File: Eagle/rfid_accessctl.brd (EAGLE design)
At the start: 50 x 40 mm, 21 parts

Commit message: Start v1.2 board version
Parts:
- removed U$1: V_REG_LD1117VXX, SparkFun-PowerIC:78XXL
- added D1, D2: (no value), SparkFun-DiscreteSemi:SMA-DIODE
- added JMP1: 0R-JUMPB, jump-0r-smd:B0R-JMP
- added Q1: IRLL014, Misc_Transistors:SOT-223
- added R6: (no value), SparkFun-Resistors:0805
- added VR1: UA78M33CDCY, TI-UA78M33CDCY:SOT230P700X180-4N
- C1: value (none) -> 0.33uF; device SparkFun-Capacitors:CPOL-RADIAL-10UF-25V-KIT -> SparkFun-Capacitors:0805
- C2: value (none) -> 0.1uF; device SparkFun-Capacitors:CAP-PTH-SMALL-KIT -> SparkFun-Capacitors:0805
- R5: value 470 -> 4.7k
- moved RELAY_HEADER 30.2 mm to (9.53, 10.2)
- moved C1 15.9 mm to (3.81, 16.5)
- moved C2 13.1 mm to (8.89, 16.5), turned to 180 degrees
- moved I2C_CONN 2.54 mm to (15.2, 30.5)
- moved R2 1.27 mm to (41.9, 20.3)
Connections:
- new net RELAY_OP: D2.A, Q1.2, RELAY_HEADER.1
- new net RELAY_PWR: D2.C, JMP1.2, RELAY_HEADER.3
- net GND: now also D1.A, LED_HEADER.3, Q1.3, R6.1, VR1.2, VR1.4; no longer LED_HEADER.2, U$1.IN
- net PWR_IN: now also C1.1, D1.C, JMP1.3, VR1.1; no longer C2.1, RELAY_HEADER.3, U$1.OUT
- net RELAY_CTL: now also Q1.1, R6.2; no longer RELAY_HEADER.1
- net VCC: now also C2.1, JMP1.1, LED_HEADER.2, VR1.3; no longer C1.1, LED_HEADER.3, U$1.GND
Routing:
- net GND: track 6.34 -> 26.2 mm, vias 1 -> 4
- net RELAY_OP: track 0.00 -> 17.3 mm, vias 0 -> 1
- net RELAY_PWR: track 0.00 -> 11.3 mm
- net PWR_IN: track 32.5 -> 21.7 mm, vias 1 -> 0
- net RELAY_CTL: track 22.9 -> 29.1 mm, vias 0 -> 2
- net SCL: track 34.7 -> 40.1 mm, vias 0 -> 2
- net VCC: track 109.0 -> 112.2 mm
- net SDA: track 31.1 -> 28.5 mm
- net PGM_CTL: track 4.76 -> 5.80 mm
- net RFID_SCK: track 18.9 -> 18.4 mm
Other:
- board text added: "3v3"
- board text added: "Access Controller V1.2"
- board text added: "Di"
- board text added: "JP1"
- board text added: "PWR_IN"
- board text added: "S'NOID/RLY"
- board text removed: "3v"
- board text removed: "Access Controller V1.1"
- board text removed: "DATA"
- board text removed: "PWR"
- board text removed: "RELAY"

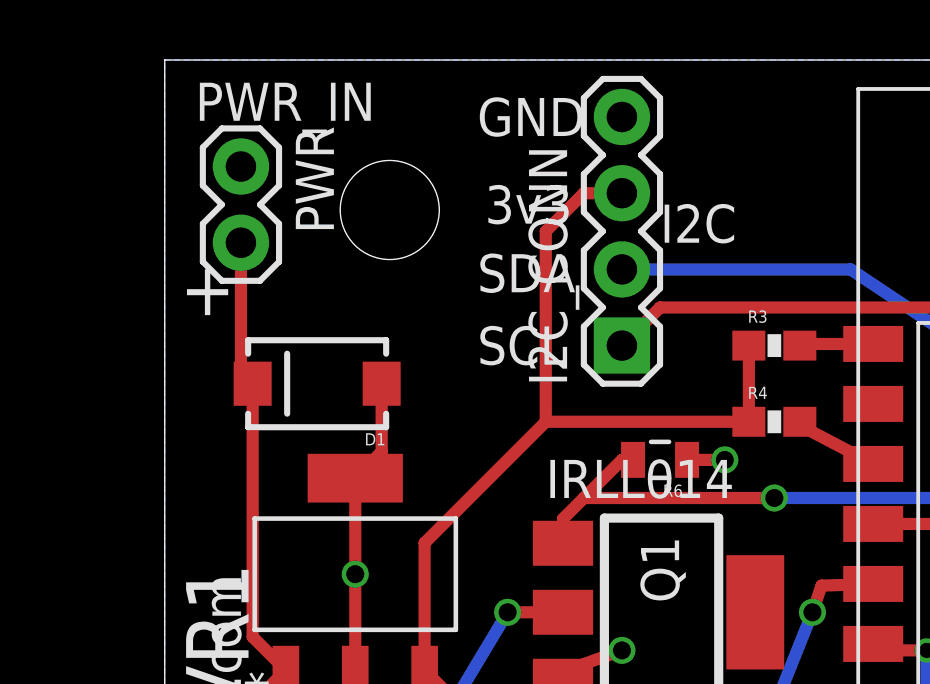
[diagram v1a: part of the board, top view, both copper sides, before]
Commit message: Updates for 0603
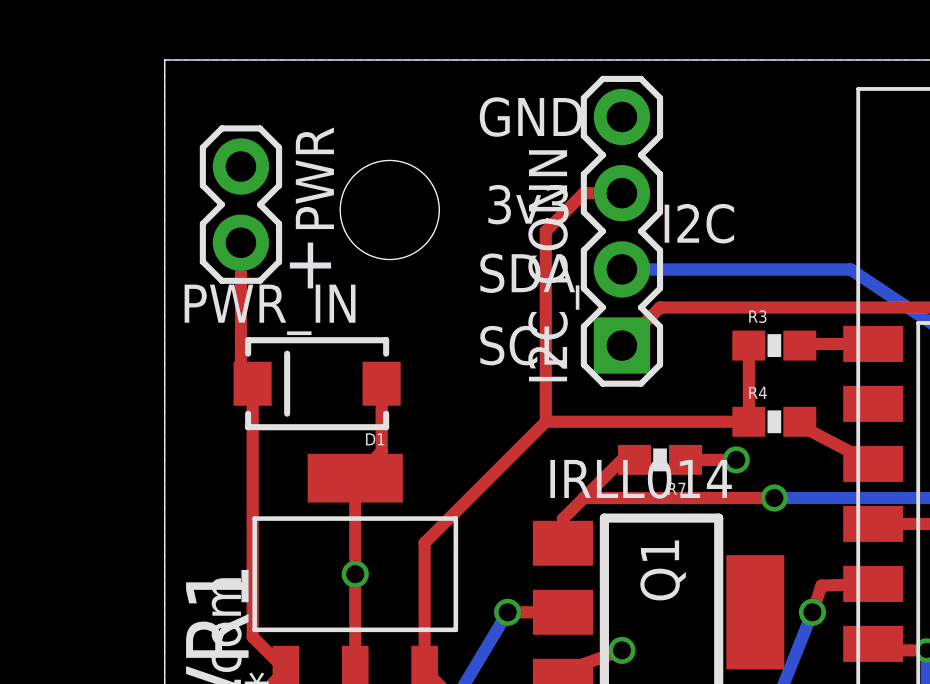
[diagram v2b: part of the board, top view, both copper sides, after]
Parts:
- removed R6: (no value), SparkFun-Resistors:0805
- added R7: (no value), SparkFun-Passives:0603-RES
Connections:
- net GND: now also R7.1; no longer R6.1
- net RELAY_CTL: now also R7.2; no longer R6.2
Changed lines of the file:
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@@
 <text x="32.385" y="9.271" size="1.27" layer="21" font="vector" ratio="15" rot="R90">RST</text>
 <text x="27.178" y="9.271" size="1.27" layer="21" font="vector" ratio="15" rot="R90">IRQ</text>
-<text x="1.016" y="37.973" size="1.27" layer="21" font="vector" ratio="15">PWR_IN</text>
-<text x="0.508" y="31.496" size="1.778" layer="21" font="vector" ratio="15">+</text>
+<text x="0.508" y="31.242" size="1.27" layer="21" font="vector" ratio="15">PWR_IN</text>
+<text x="3.937" y="32.385" size="1.778" layer="21" font="vector" ratio="15">+</text>
 <text x="3.048" y="7.239" size="1.27" layer="21" font="vector" ratio="15">S'NOID/RLY</text>
 <text x="16.51" y="33.909" size="1.27" layer="21" font="vector" ratio="15">I2C</text>
@@
 <element name="D1" library="SparkFun-DiscreteSemi" package="SMA-DIODE" value="" x="5.08" y="29.21" rot="R180"/>
 <element name="D2" library="SparkFun-DiscreteSemi" package="SMA-DIODE" value="" x="12.7" y="11.43" rot="R90"/>
-<element name="R6" library="SparkFun-Resistors" package="0805" value="" x="16.51" y="26.67" rot="R180"/>
+<element name="R7" library="SparkFun-Passives" package="0603-RES" value="" x="16.51" y="26.67" rot="R180"/>
 </elements>
 <signals>
@@
 <wire x1="6.35" y1="22.86" x2="6.35" y2="26.0604" width="0.4064" layer="1"/>
 <contactref element="RELAY_HEADER" pad="2"/>
-<contactref element="R6" pad="1"/>
-<via x="18.669" y="26.67" extent="1-16" drill="0.6"/>
-<wire x1="17.41" y1="26.67" x2="18.669" y2="26.67" width="0.4064" layer="1"/>
 <contactref element="LED_HEADER" pad="3"/>
+<contactref element="R7" pad="1"/>
+<via x="19.05" y="26.67" extent="1-16" drill="0.6"/>
+<wire x1="17.36" y1="26.67" x2="19.05" y2="26.67" width="0.4064" layer="1"/>
 </signal>
 <signal name="PWR_IN">
@@
 <wire x1="13.97" y1="25.4" x2="13.275" y2="24.705" width="0.4064" layer="1"/>
 <wire x1="13.275" y1="24.705" x2="13.275" y2="23.89" width="0.4064" layer="1"/>
-<contactref element="R6" pad="2"/>
-<wire x1="15.61" y1="26.67" x2="15.24" y2="26.67" width="0.4064" layer="1"/>
+<contactref element="R7" pad="2"/>
+<wire x1="15.66" y1="26.67" x2="15.24" y2="26.67" width="0.4064" layer="1"/>
 <wire x1="15.24" y1="26.67" x2="13.97" y2="25.4" width="0.4064" layer="1"/>
 </signal>

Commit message: Add DIP switches on serial lines (optional)
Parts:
- added SW1: (no value), SparkFun-Electromechanical:DIPSWITCH-02-50MIL
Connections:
- net GND: now also SW1.3, SW1.4
- net RXD: now also SW1.1
- net TXD: now also SW1.2
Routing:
- net TXD: track 11.8 -> 32.3 mm, vias 0 -> 2
- net RXD: track 11.5 -> 28.9 mm, vias 0 -> 2
- net GND: track 26.6 -> 29.3 mm, vias 4 -> 5
- net VCC: track 112.2 -> 114.0 mm, vias 2 -> 1
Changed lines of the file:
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@@
 <element name="D2" library="SparkFun-DiscreteSemi" package="SMA-DIODE" value="" x="12.7" y="11.43" rot="R90"/>
 <element name="R7" library="SparkFun-Passives" package="0603-RES" value="" x="16.51" y="26.67" rot="R180"/>
+<element name="SW1" library="SparkFun-Electromechanical" package="DIPSWITCH-02-50MIL" value="" x="38.1" y="10.16" rot="R180"/>
 </elements>
 <signals>
@@
 <via x="19.05" y="26.67" extent="1-16" drill="0.6"/>
 <wire x1="17.36" y1="26.67" x2="19.05" y2="26.67" width="0.4064" layer="1"/>
+<contactref element="SW1" pad="4"/>
+<contactref element="SW1" pad="3"/>
+<wire x1="38.735" y1="6.46" x2="38.1" y2="6.46" width="0.4064" layer="1"/>
+<via x="38.1" y="5.08" extent="1-16" drill="0.6"/>
+<wire x1="38.1" y1="6.46" x2="37.465" y2="6.46" width="0.4064" layer="1"/>
+<wire x1="38.1" y1="5.08" x2="38.1" y2="6.46" width="0.4064" layer="1"/>
 </signal>
 <signal name="PWR_IN">
@@
 <contactref element="RFID_CONN" pad="8"/>
 <wire x1="19.47" y1="30.48" x2="19.47" y2="27.94" width="0.4064" layer="1"/>
-<via x="34.29" y="15.24" extent="1-16" drill="0.508"/>
-<wire x1="48.26" y1="30.48" x2="46.99" y2="30.48" width="0.4064" layer="1"/>
-<wire x1="46.99" y1="30.48" x2="44.45" y2="27.94" width="0.4064" layer="1"/>
-<wire x1="44.45" y1="27.94" x2="44.45" y2="24.13" width="0.4064" layer="1"/>
-<via x="44.45" y="24.13" extent="1-16" drill="0.508"/>
-<wire x1="44.45" y1="24.13" x2="44.45" y2="17.78" width="0.4064" layer="16"/>
-<wire x1="44.45" y1="17.78" x2="45.72" y2="16.51" width="0.4064" layer="16"/>
-<wire x1="45.72" y1="16.51" x2="48.26" y2="16.51" width="0.4064" layer="16"/>
 <contactref element="X1" pad="8"/>
 <contactref element="I2C_CONN" pad="3"/>
-<wire x1="34.29" y1="6.35" x2="34.29" y2="15.24" width="0.4064" layer="1"/>
-<wire x1="23.615" y1="16.535" x2="25.375" y2="16.535" width="0.4064" layer="1"/>
-<wire x1="25.375" y1="16.535" x2="29.21" y2="15.24" width="0.4064" layer="1"/>
-<wire x1="29.21" y1="15.24" x2="34.29" y2="15.24" width="0.4064" layer="1"/>
 <contactref element="R5" pad="2"/>
-<wire x1="44.45" y1="17.78" x2="44.45" y2="15.24" width="0.4064" layer="16"/>
-<wire x1="44.45" y1="15.24" x2="41.91" y2="15.24" width="0.4064" layer="16"/>
-<wire x1="41.91" y1="15.24" x2="34.29" y2="15.24" width="0.4064" layer="16"/>
-<wire x1="42.887" y1="24.638" x2="43.942" y2="24.638" width="0.4064" layer="1"/>
-<wire x1="43.942" y1="24.638" x2="44.45" y2="24.13" width="0.4064" layer="1"/>
 <contactref element="VR1" pad="3"/>
 <contactref element="C2" pad="1"/>
@@
 <wire x1="8.6614" y1="23.9014" x2="12.7" y2="27.94" width="0.4064" layer="1"/>
 <contactref element="LED_HEADER" pad="2"/>
-<wire x1="48.26" y1="10.16" x2="45.72" y2="10.16" width="0.4064" layer="16"/>
-<wire x1="45.72" y1="10.16" x2="41.91" y2="13.97" width="0.4064" layer="16"/>
-<wire x1="41.91" y1="13.97" x2="41.91" y2="15.24" width="0.4064" layer="16"/>
+<wire x1="23.615" y1="16.535" x2="30.455" y2="16.535" width="0.4064" layer="1"/>
+<wire x1="30.455" y1="16.535" x2="34.29" y2="12.7" width="0.4064" layer="1"/>
+<wire x1="34.29" y1="12.7" x2="34.29" y2="6.35" width="0.4064" layer="1"/>
+<wire x1="48.26" y1="10.16" x2="38.1" y2="10.16" width="0.4064" layer="1"/>
+<wire x1="38.1" y1="10.16" x2="34.29" y2="6.35" width="0.4064" layer="1"/>
+<wire x1="48.26" y1="10.16" x2="46.99" y2="10.16" width="0.4064" layer="16"/>
+<wire x1="46.99" y1="10.16" x2="45.72" y2="11.43" width="0.4064" layer="16"/>
+<wire x1="45.72" y1="11.43" x2="45.72" y2="15.24" width="0.4064" layer="16"/>
+<wire x1="45.72" y1="15.24" x2="46.99" y2="16.51" width="0.4064" layer="16"/>
+<wire x1="46.99" y1="16.51" x2="48.26" y2="16.51" width="0.4064" layer="16"/>
+<wire x1="48.26" y1="30.48" x2="46.99" y2="30.48" width="0.4064" layer="1"/>
+<wire x1="46.99" y1="30.48" x2="43.18" y2="26.67" width="0.4064" layer="1"/>
+<wire x1="43.18" y1="26.67" x2="43.18" y2="24.931" width="0.4064" layer="1"/>
+<wire x1="43.18" y1="24.931" x2="42.887" y2="24.638" width="0.4064" layer="1"/>
+<wire x1="42.887" y1="24.638" x2="45.212" y2="24.638" width="0.4064" layer="1"/>
+<wire x1="45.212" y1="24.638" x2="45.72" y2="24.13" width="0.4064" layer="1"/>
+<wire x1="45.72" y1="24.13" x2="45.72" y2="20.32" width="0.4064" layer="1"/>
+<via x="45.72" y="20.32" extent="1-16" drill="0.6"/>
+<wire x1="45.72" y1="20.32" x2="45.72" y2="19.05" width="0.4064" layer="16"/>
+<wire x1="45.72" y1="19.05" x2="48.26" y2="16.51" width="0.4064" layer="16"/>
 </signal>
 <signal name="DTR">
@@
 <signal name="RXD">
 <contactref element="FTDI_CONN" pad="TXO"/>
+<wire x1="43.775" y1="28.535" x2="48.26" y2="33.02" width="0.4064" layer="1"/>
+<contactref element="SW1" pad="1"/>
 <contactref element="X1" pad="15"/>
-<wire x1="38.615" y1="28.535" x2="43.775" y2="28.535" width="0.4064" layer="1"/>
-<wire x1="43.775" y1="28.535" x2="48.26" y2="33.02" width="0.4064" layer="1"/>
+<wire x1="43.775" y1="28.535" x2="38.615" y2="28.535" width="0.4064" layer="1"/>
+<wire x1="38.615" y1="28.535" x2="37.425" y2="28.535" width="0.4064" layer="1"/>
+<wire x1="37.425" y1="28.535" x2="36.83" y2="27.94" width="0.4064" layer="1"/>
+<via x="36.83" y="27.94" extent="1-16" drill="0.6"/>
+<wire x1="36.83" y1="27.94" x2="36.83" y2="24.13" width="0.4064" layer="16"/>
+<wire x1="36.83" y1="24.13" x2="38.1" y2="22.86" width="0.4064" layer="16"/>
+<wire x1="38.1" y1="22.86" x2="38.1" y2="16.51" width="0.4064" layer="16"/>
+<wire x1="38.1" y1="16.51" x2="39.37" y2="15.24" width="0.4064" layer="16"/>
+<via x="39.37" y="15.24" extent="1-16" drill="0.6"/>
+<wire x1="39.37" y1="15.24" x2="39.37" y2="14.495" width="0.4064" layer="1"/>
+<wire x1="39.37" y1="14.495" x2="38.735" y2="13.86" width="0.4064" layer="1"/>
 </signal>
 <signal name="TXD">
 <contactref element="FTDI_CONN" pad="RXI"/>
-<contactref element="X1" pad="16"/>
-<wire x1="38.615" y1="30.535" x2="43.125" y2="30.535" width="0.4064" layer="1"/>
 <wire x1="43.125" y1="30.535" x2="43.18" y2="30.48" width="0.4064" layer="1"/>
 <wire x1="43.18" y1="30.48" x2="48.26" y2="35.56" width="0.4064" layer="1"/>
+<contactref element="X1" pad="16"/>
+<contactref element="SW1" pad="2"/>
+<wire x1="43.125" y1="30.535" x2="38.615" y2="30.535" width="0.4064" layer="1"/>
+<wire x1="38.615" y1="30.535" x2="35.615" y2="30.535" width="0.4064" layer="1"/>
+<wire x1="35.615" y1="30.535" x2="35.56" y2="30.48" width="0.4064" layer="1"/>
+<via x="35.56" y="30.48" extent="1-16" drill="0.6"/>
+<wire x1="35.56" y1="30.48" x2="35.56" y2="22.86" width="0.4064" layer="16"/>
+<wire x1="35.56" y1="22.86" x2="36.83" y2="21.59" width="0.4064" layer="16"/>
+<wire x1="36.83" y1="21.59" x2="36.83" y2="15.24" width="0.4064" layer="16"/>
+<via x="36.83" y="15.24" extent="1-16" drill="0.6"/>
+<wire x1="36.83" y1="15.24" x2="36.83" y2="14.495" width="0.4064" layer="1"/>
+<wire x1="36.83" y1="14.495" x2="37.465" y2="13.86" width="0.4064" layer="1"/>
 </signal>
 <signal name="PGM_CTL">
@@
 <contactref element="Q1" pad="1"/>
 <via x="20.32" y="25.4" extent="1-16" drill="0.6"/>
-<wire x1="20.32" y1="25.4" x2="31.75" y2="25.4" width="0.4064" layer="16"/>
-<via x="31.75" y="25.4" extent="1-16" drill="0.6"/>
-<wire x1="31.75" y1="25.4" x2="32.885" y2="26.535" width="0.4064" layer="1"/>
+<wire x1="20.32" y1="25.4" x2="30.48" y2="25.4" width="0.4064" layer="16"/>
+<via x="30.48" y="25.4" extent="1-16" drill="0.6"/>
+<wire x1="30.48" y1="25.4" x2="32.885" y2="26.535" width="0.4064" layer="1"/>
 <wire x1="32.885" y1="26.535" x2="38.615" y2="26.535" width="0.4064" layer="1"/>
 <wire x1="20.32" y1="25.4" x2="13.97" y2="25.4" width="0.4064" layer="1"/>
@@
 <signal name="SDA">
 <contactref element="I2C_CONN" pad="2"/>
-<wire x1="15.24" y1="33.02" x2="22.86" y2="33.02" width="0.4064" layer="16"/>
-<wire x1="22.86" y1="33.02" x2="35.433" y2="24.638" width="0.4064" layer="16"/>
-<via x="35.433" y="24.638" extent="1-16" drill="0.508"/>
+<wire x1="15.24" y1="33.02" x2="24.13" y2="33.02" width="0.4064" layer="16"/>
+<wire x1="24.13" y1="33.02" x2="34.163" y2="24.638" width="0.4064" layer="16"/>
+<via x="34.163" y="24.638" extent="1-16" drill="0.508"/>
 <contactref element="X1" pad="13"/>
 <contactref element="R5" pad="1"/>
 <wire x1="38.615" y1="24.535" x2="35.56" y2="24.535" width="0.4064" layer="1"/>
-<wire x1="35.56" y1="24.535" x2="35.433" y2="24.638" width="0.4064" layer="1"/>
+<wire x1="35.56" y1="24.535" x2="34.163" y2="24.638" width="0.4064" layer="1"/>
 <wire x1="41.187" y1="24.638" x2="38.925" y2="24.535" width="0.4064" layer="1"/>
 <wire x1="38.925" y1="24.535" x2="38.615" y2="24.535" width="0.4064" layer="1"/>
